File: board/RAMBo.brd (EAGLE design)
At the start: 104.1 x 102.9 mm, 257 parts, among them Q1 PSMN7R0-60YS, Q2 PSMN7R0-60YS, Q3 PSMN7R0-60YS, Q4 IRLML6346TRPBF, Q5 PSMN7R0-60YS, Q8 IRLML6346TRPBF, U1 ATMEGA32U2-MUR, U2 ATMEGA2560-16AU, U3 TPS54332DDA, U4 AD5206, U5 A4982, U6 A4982, U7 A4982, U8 A4982, U9 A4982, X1 C-GRID-02-70543, X10 C-GRID-04-70543, X11 MSTBV10, X12 SPI, X13 EXT-2, X14 C-GRID-04-70543, X15 C-GRID-04-70543, X16 32u2 EXT, X17 3x2M, X18 3x2M, X19 Analog-Ext, X2 USB B-TH, X20 M05PTH, X21 C-GRID-03-70543, X22 C-GRID-03-70543, X23 C-GRID-03-70543, X24 C-GRID-03-70543, X25 C-GRID-03-70543, X26 C-GRID-03-70543, X27 C-GRID-02-70543, X28 C-GRID-02-70543, X29 C-GRID-02-70543, X3 C-GRID-02-70543, X30 C-GRID-02-70543, X31 M05PTH, X32 M05PTH, X33 MSTBA6, X34 PWM_EXT, X39 M05X2PTH, X4 C-GRID-04-70543, X5 C-GRID-02-70543, X6 C-GRID-04-70543, X7 C-GRID-04-70543, X8 C-GRID-04-70543, X9 C-GRID-02-70543, Y1 16MHz KX-7, Y2 16MHz KX-7

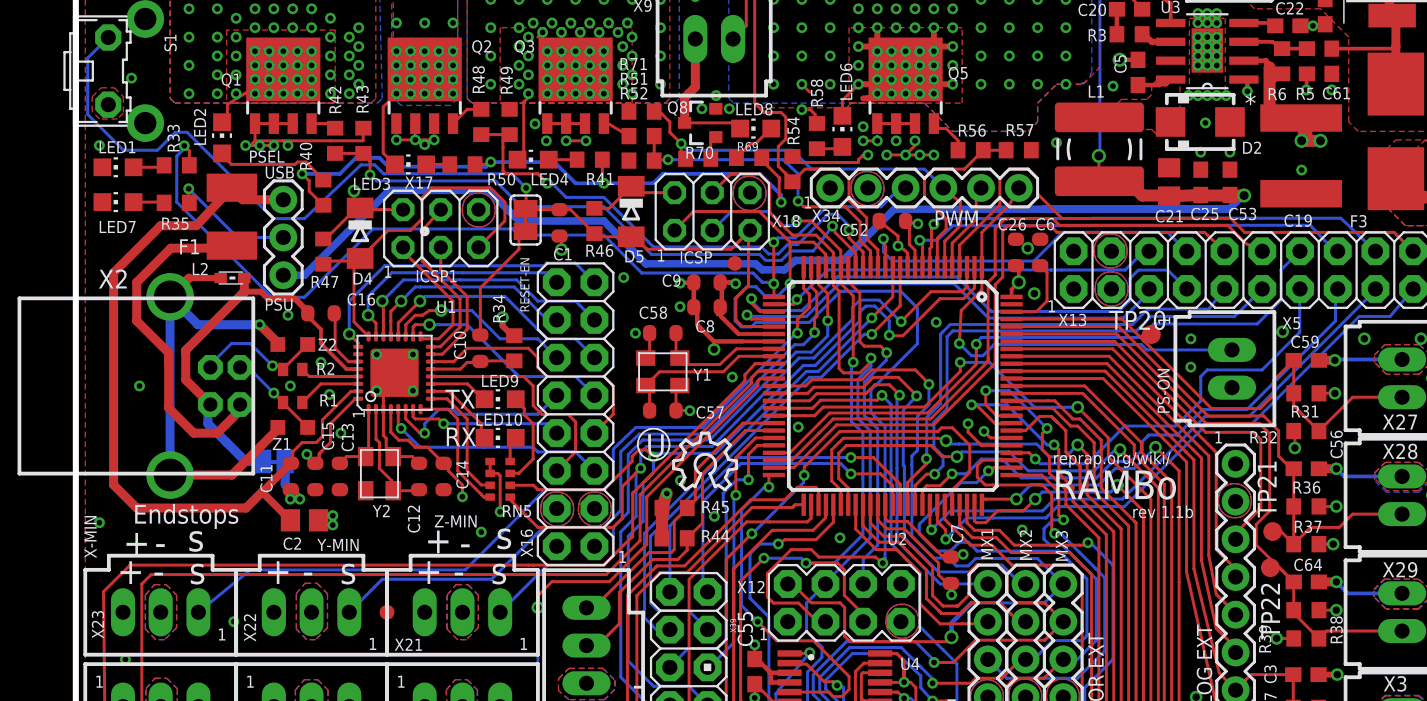
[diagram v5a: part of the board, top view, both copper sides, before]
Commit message: change SMA package size
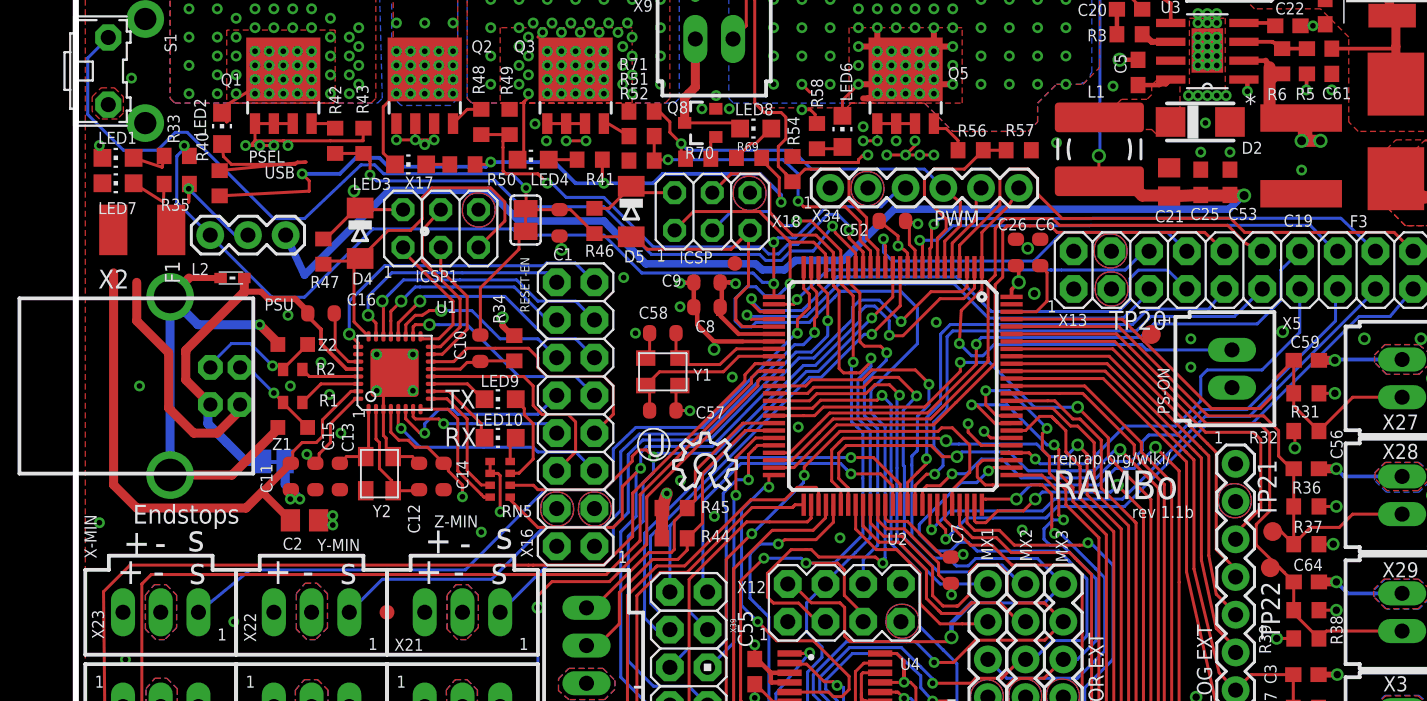
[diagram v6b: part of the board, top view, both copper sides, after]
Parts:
- D2: device ultimachine1:SMA -> ultimachine1:SMA-SM
- moved R40 7.01 mm to (9.68, 72.1)
- moved F1 6.10 mm to (4.47, 68.9), turned to 0 degrees
- moved JP1 2.70 mm to (14.1, 68.6), turned to 180 degrees
- moved LED7 1.27 mm to (2.84, 72.1)
- moved R35 1.27 mm to (6.80, 72.0)
- moved LED1 0.64 mm to (2.84, 73.8)
- moved LED2 0.64 mm to (9.84, 75.8)
- moved R33 0.64 mm to (6.79, 73.9)
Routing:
- net PS_5V: track 122.1 -> 98.7 mm
- net USBVCC: track 54.3 -> 40.1 mm
- net XVCC: track 24.0 -> 15.9 mm
- net N$84: track 7.76 -> 12.5 mm
- net +12V2: track 126.2 -> 128.8 mm
- net N$3: track 2.08 -> 3.60 mm
- net VCC: track 93.3 -> 92.1 mm
- net L13: track 65.9 -> 65.2 mm
- net N$2: track 2.11 -> 2.80 mm

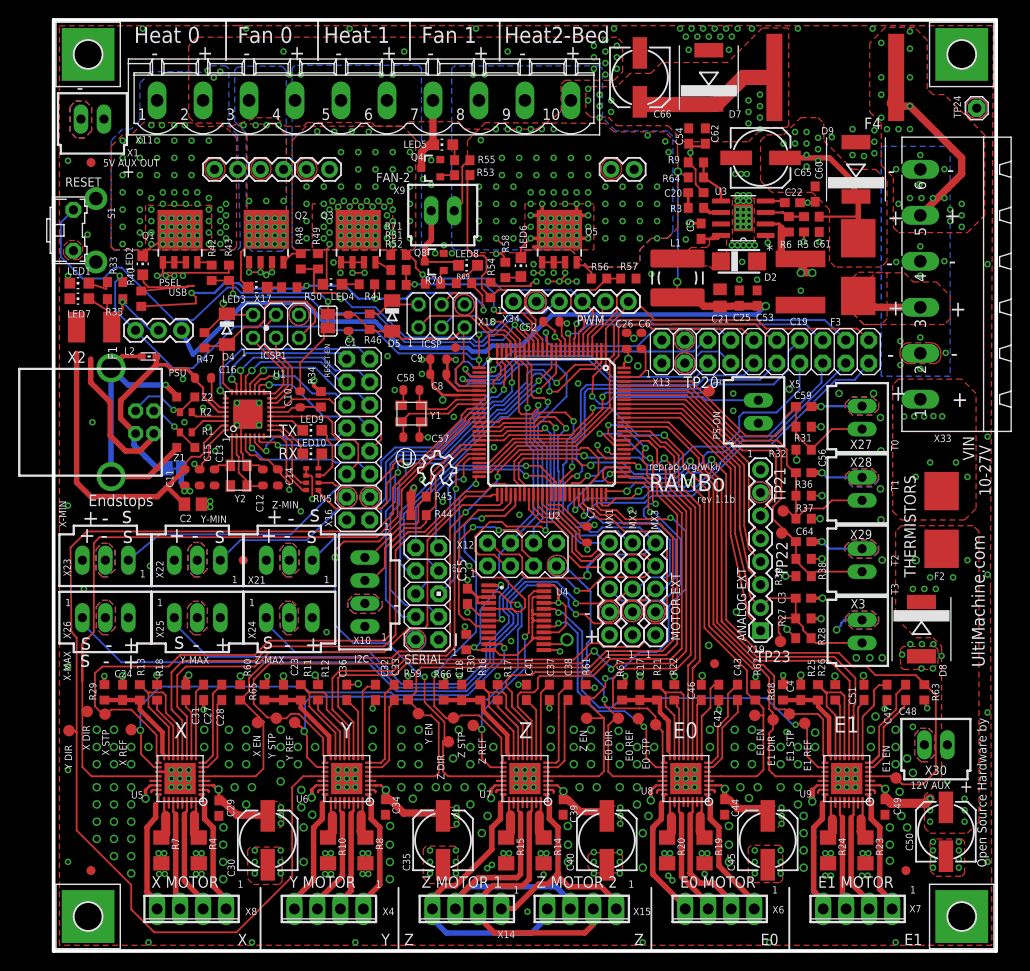
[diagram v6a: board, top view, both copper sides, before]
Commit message: add freewheeling diodes, working on 32u2 layout,
start adding icoupler
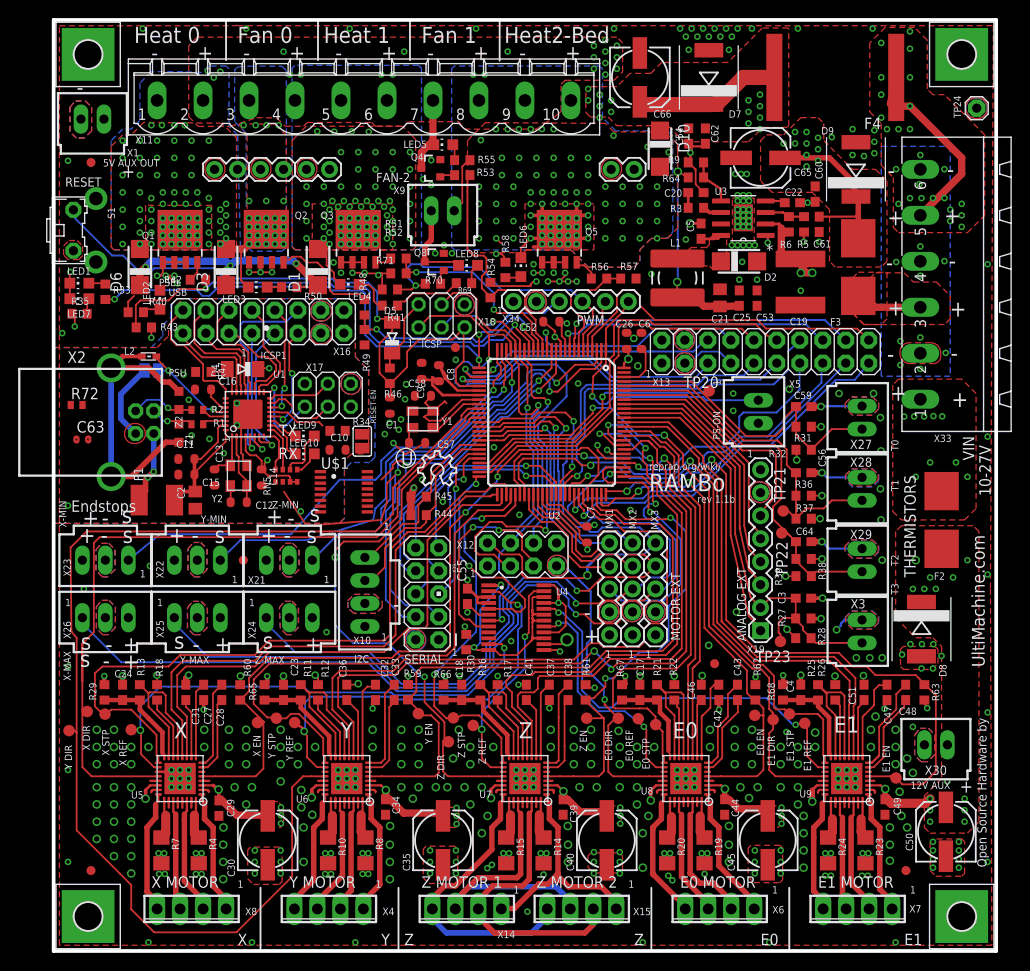
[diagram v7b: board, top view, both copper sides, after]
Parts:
- removed JP1: (no value), SparkFun:1X03
- added C63: 4.7nF, SmartPrj:C0402
- added D1, D10, D3, D6: B240A-13-F, ultimachine1:SMA-SM
- added R72: 1M, rcl:R0402
- added U$1: ADUM7441, ultimachine:QSOP16
- moved X16 23.4 mm to (32.1, 70.8), turned to 180 degrees
- moved F1 20.3 mm to (11.4, 49.8), turned to 180 degrees
- moved JP2 13.8 mm to (34.1, 56.3), turned to 90 degrees
- moved R43 11.2 mm to (9.97, 68.9), turned to 0 degrees
- moved JP3 11.1 mm to (10.8, 64.1), turned to 0 degrees
- moved C1 10.2 mm to (37.1, 60.3)
- moved R49 9.83 mm to (34.4, 67.8), turned to 270 degrees
- moved X17 9.53 mm to (30.3, 61.4)
- moved R48 8.69 mm to (34.4, 71.1)
- moved C10 6.95 mm to (31.4, 55.4), turned to 0 degrees
- moved R46 6.37 mm to (37.1, 63.6)
- moved D4 4.75 mm to (20.9, 64.3), turned to 180 degrees
- moved LED2 4.26 mm to (11.7, 72.0)
- moved R35 4.26 mm to (2.86, 70.4), turned to 0 degrees
- moved R34 3.95 mm to (31.4, 57.5), turned to 0 degrees
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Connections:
- removed net PS_5V: C21.1, C25.1, C53.1, JP1.1, L1.2, R64.2
- new net GND1: C11.2, C12.2, C13.2, C14.2, C15.2, C16.2, C2.1, JP3.2, R34.2, U1.3, U1.33, X16.3, X16.4, X17.6, X2.4, Y2.2, Y2.4
- new net N$120: U$1.6
- new net N$121: U$1.14
- new net N$131: U$1.13
- new net N$142: U$1.12
- new net N$153: U$1.11
- new net N$87: C10.2, JP2.1
- new net N$89: U$1.3
- new net N$91: U$1.5
- net +12V2: now also D1.C, D3.C, D6.C
- net +12V3: now also D10.C
- net GND: no longer C11.2, C12.2, C13.2, C14.2, C15.2, C2.1, JP3.2, R34.2, U1.3, U1.33, X16.3, X16.4, X17.6, Y2.2, Y2.4
- net N$101: now also D1.A
- net N$107: now also D10.A
- net N$11: now also C63.2, R72.1; no longer C16.2, X2.4
- net N$21: now also D6.A
- net N$54: now also LED9.A, RN5.6; no longer LED10.A, RN5.4
- net N$55: now also LED10.A, RN5.5; no longer LED9.A, RN5.3
- net N$98: now also D3.A
- net RESET: no longer C10.2, JP2.1
- net USBVCC: now also C14.1, C15.1, D4.C, R47.2, RN5.3, RN5.4, U1.32, U1.4, X16.1, X16.2, X17.2; no longer JP1.3
- net USHIELD: now also R72.2
- net VCC: now also C21.1, C25.1, C53.1, L1.2, R64.2; no longer C14.1, C15.1, D4.C, JP1.2, R47.2, RN5.5, RN5.6, U1.32, U1.4, X16.1, X16.2, X17.2
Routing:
- net PS_5V: track 98.7 -> 0.00 mm, vias 3 -> 0
- net RESET2: track 26.0 -> 4.68 mm
- net GND1: track 0.00 -> 17.6 mm, vias 0 -> 7
- net N$11: track 27.6 -> 11.5 mm, vias 0 -> 2
- net HEAT-0: track 41.5 -> 56.5 mm
- net +12V2: track 128.8 -> 114.4 mm
- net GND: track 158.4 -> 144.2 mm, vias 473 -> 459
- net N$84: track 12.5 -> 1.96 mm
- net FAN-0: track 34.8 -> 24.7 mm
- net N$26: track 2.30 -> 12.2 mm
- net VCC: track 92.1 -> 82.5 mm, vias 27 -> 25
- net USBVCC: track 40.1 -> 30.7 mm, vias 0 -> 2
- net RX0: track 62.6 -> 55.3 mm
- net U1-PC5: track 21.4 -> 14.1 mm, vias 1 -> 0
- net U1-PC2: track 15.6 -> 22.6 mm
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- added copper zone on layer 1, net GND1
- added copper zone on layer 15, net GND1
- added copper zone on layer 16, net GND1
- added copper zone on layer 2, net GND1
- added copper zone on layer 15, net N$95
- added copper zone on layer 15, net USBVCC
- removed copper zone on layer 15, net GND

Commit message: finish icoupler addition, remove ps-select jumper
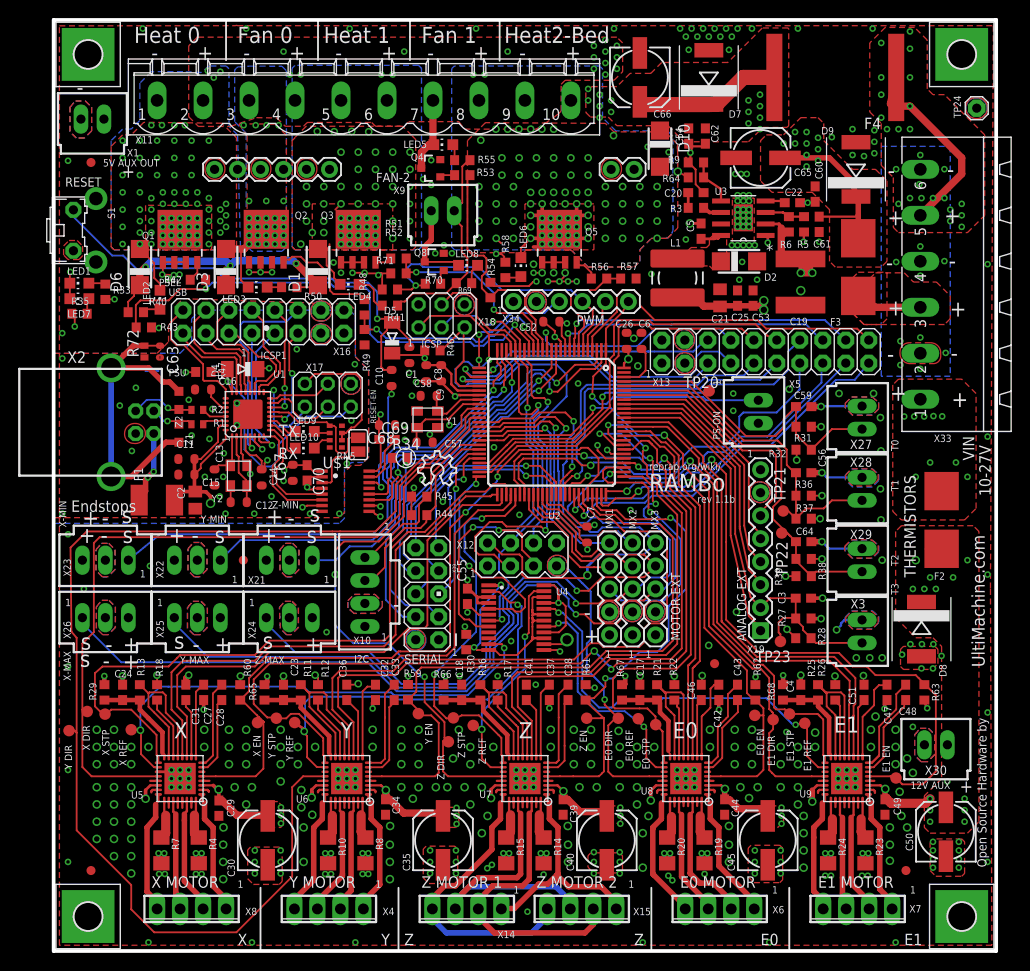
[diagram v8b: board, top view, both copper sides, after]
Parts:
- removed FID3: FIDUCIAL1X2, SparkFun:FIDUCIAL-1X2
- removed JP3: (no value), ultimachine:SJ-NOSTOP
- removed L2: MH2029-300Y, wuerth-elektronik:0603
- added C67, C68: 100nF, SmartPrj:C0603-ROUND
- added C69, C70: 10nF, rcl:C0603
- R40, R41, R50, R55, R58, R69: value 1K -> 1.8K
- moved C63 13.0 mm to (11.7, 66.2), turned to 270 degrees
- moved C10 9.93 mm to (37.3, 63.3), turned to 90 degrees
- moved R72 9.54 mm to (10.0, 66.2), turned to 90 degrees
- moved R34 7.54 mm to (38.3, 54.5)
- moved RN5 6.96 mm to (31.2, 56.8), turned to 90 degrees
- moved C1 5.99 mm to (39.3, 65.8)
- moved R46 5.47 mm to (41.8, 66.4), turned to 180 degrees
- moved C9 2.17 mm to (42.8, 63.8)
- moved C8 1.40 mm to (41.2, 63.8)
- moved C57 0.83 mm to (41.0, 56.2)
- moved C58 0.64 mm to (41.4, 61.3)
- moved LED10 0.63 mm to (27.7, 55.6)
- moved JP2 0.59 mm to (33.7, 55.9), turned to 270 degrees
- moved LED9 0.51 mm to (27.7, 57.4)
- moved Y1 0.51 mm to (41.3, 58.7)
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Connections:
- removed net M8RXD: RN5.7, U1.9
- removed net M8TXD: RN5.8, U1.8
- removed net N$120: U$1.6
- removed net N$121: U$1.14
- removed net N$131: U$1.13
- removed net N$142: U$1.12
- removed net N$153: U$1.11
- removed net N$87: C10.2, JP2.1
- removed net N$89: U$1.3
- removed net N$91: U$1.5
- new net RESET-I: JP2.2, U$1.3
- new net RST-IO: C10.1, U$1.14
- new net RX0-I: U$1.5, U1.9
- new net TX0-I: U$1.6, U1.8
- net DTR: now also JP2.1, RN5.5; no longer C10.1, R34.1
- net GND: now also C68.1, C69.2, U$1.15, U$1.9
- net GND1: now also C63.2, C67.1, C70.2, R72.1, RN5.4, U$1.2, U$1.4, U$1.8, U1.28; no longer JP3.2, R34.2
- net N$11: now also LED10.A, RN5.7; no longer C63.2, JP3.1, L2.1, R72.1, U1.28
- net N$55: now also R34.1, U$1.12; no longer LED10.A, RN5.5
- net RESET: now also C10.2; no longer JP2.2
- net RX0: now also R34.2; no longer RN5.2
- net TX0: now also U$1.11; no longer RN5.1
- net USBVCC: now also C67.2, C70.1, RN5.2, U$1.1, U$1.7; no longer RN5.4
- net USHIELD: now also C63.1; no longer L2.2
- net VCC: now also C68.2, C69.1, U$1.10, U$1.16
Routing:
- net L13: track 62.7 -> 15.4 mm
- net RESET2: track 4.68 -> 30.4 mm, vias 0 -> 1
- net USBVCC: track 30.7 -> 52.0 mm, vias 2 -> 6
- net RST-IO: track 0.00 -> 13.4 mm, vias 0 -> 2
- net TX0-I: track 0.00 -> 13.2 mm
- net TX0: track 68.1 -> 55.4 mm
- net RX0-I: track 0.00 -> 12.6 mm
- net +12V2: track 114.4 -> 125.0 mm
- net N$11: track 11.5 -> 2.06 mm, vias 2 -> 0
- net DTR: track 6.43 -> 14.6 mm
- net RESET-I: track 0.00 -> 6.72 mm
- net N$21: track 0.00 -> 5.48 mm, vias 75 -> 73
- net M8TXD: track 5.23 -> 0.00 mm
- net M8RXD: track 5.23 -> 0.00 mm
- net GND1: track 17.6 -> 12.5 mm, vias 7 -> 27
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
